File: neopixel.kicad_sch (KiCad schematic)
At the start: 1 part

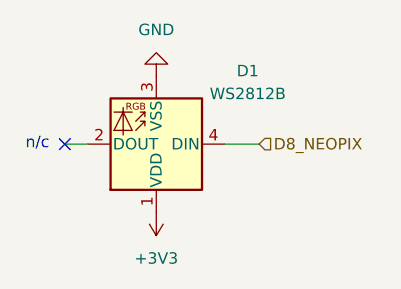
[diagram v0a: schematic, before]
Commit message: Adding symbols information
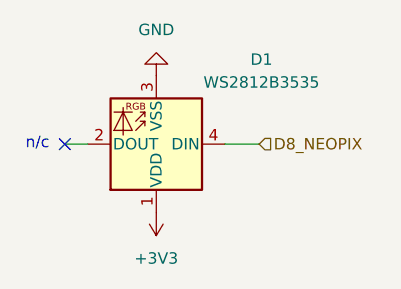
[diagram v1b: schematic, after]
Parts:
- D1: value WS2812B -> WS2812B3535; footprint LED_SMD:LED_WS2812B_PLCC4_5.0x5.0mm_P3.2mm -> LED_SMD:LED_SK6812MINI_PLCC4_3.5x3.5mm_P1.75mm; Mfr (none) -> DONGGUANG OPSCO OPTOELECTRONICS CO., LTD; Mfr P/N (none) -> SK6812MINI; Supplier_1 (none) -> Adafruit; Supplier_1 P/N (none) -> 2686; Supplier_1 Price @ Qty (none) -> 0.446; Supplier_1 Unit Price (none) -> 0.495
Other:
- company: (none) -> catbranchman
- title: (none) -> Neopixel
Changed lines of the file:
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@@
 	(generator_version "8.0")
 	(paper "A4")
+	(title_block
+		(title "Neopixel")
+		(rev "0.1")
+		(company "catbranchman")
+		(comment 1 "Electrical Engineering Department")
+		(comment 2 "EE 156 / Stanford University")
+		(comment 3 "Flight Club, W6YX, Endurance")
+	)
 	(no_connect
 		(at 138.43 96.52)
@@
 		(dnp no)
 		(property "Reference" "D1"
-			(at 158.75 88.392 0)
+			(at 160.274 87.122 0)
 			(effects
 				(font
@@
 			)
 		)
-		(property "Value" "WS2812B"
-			(at 158.75 90.932 0)
+		(property "Value" "WS2812B3535"
+			(at 160.274 89.662 0)
 			(effects
 				(font
@@
 			)
 		)
-		(property "Footprint" "LED_SMD:LED_WS2812B_PLCC4_5.0x5.0mm_P3.2mm"
+		(property "Footprint" "LED_SMD:LED_SK6812MINI_PLCC4_3.5x3.5mm_P1.75mm"
 			(at 147.32 88.9 0)
 			(effects
@@
 			)
 		)
-		(property "Datasheet" "https://cdn-shop.adafruit.com/datasheets/WS2812B.pdf"
+		(property "Datasheet" "https://cdn-shop.adafruit.com/product-files/2686/SK6812MINI_REV.01-1-2.pdf"
 			(at 146.05 86.995 0)
 			(effects
@@
 			)
 		)
-		(property "Description" "RGB LED with integrated controller"
+		(property "Description" "NeoPixel Mini 3535 RGB LEDs w/ Integrated Driver Chip - Black"
 			(at 148.59 96.52 0)
 			(effects
+				(font
+					(size 1.27 1.27)
+				)
+				(hide yes)
+			)
+		)
+		(property "Mfr" "DONGGUANG OPSCO OPTOELECTRONICS CO., LTD"
+			(at 148.59 96.52 0)
+			(effects
+				(font
+					(size 1.27 1.27)
+				)
+				(hide yes)
+			)
+		)
+		(property "Mfr P/N" "SK6812MINI"
+			(at 148.59 96.52 0)
+			(effects
+				(font
+					(size 1.27 1.27)
+				)
+				(hide yes)
+			)
+		)
+		(property "Supplier_1" "Adafruit"
+			(at 148.59 96.52 0)
+			(effects
+				(font
+					(size 1.27 1.27)
+				)
+				(hide yes)
+			)
+		)
+		(property "Supplier_1 P/N" "2686"
+			(at 148.59 96.52 0)
+			(effects
+				(font
+					(size 1.27 1.27)
+				)
+				(hide yes)
+			)
+		)
+		(property "Supplier_1 Unit Price" "0.495"
+			(at 148.59 96.52 0)
+			(effects
+				(font
+					(size 1.27 1.27)
+				)
+				(hide yes)
+			)
+		)
+		(property "Supplier_1 Price @ Qty" "0.446"
+			(at 148.59 96.52 0)
+			(effects
+				(font
+					(size 1.27 1.27)
+				)
+				(hide yes)
+			)
+		)
+		(property "Supplier_2" ""
+			(at 148.59 96.52 0)
+			(effects
+				(font
+					(size 1.27 1.27)
+				)
+				(hide yes)
+			)
+		)
+		(property "Supplier_2 P/N" ""
+			(at 148.59 96.52 0)
+			(effects
+				(font
+					(size 1.27 1.27)
+				)
+				(hide yes)
+			)
+		)
+		(property "Supplier_2 Unit Price" ""
+			(at 148.59 96.52 0)
+			(effects
+				(font
+					(size 1.27 1.27)
+				)
+				(hide yes)
+			)
+		)
+		(property "Supplier_2 Price @ Qty" ""
+			(at 148.59 96.52 0)
+			(effects
